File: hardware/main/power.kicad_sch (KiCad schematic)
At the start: 32 parts, among them Q1 SSM3J338R, Q2 BCP53, Q3 SSM3J338R, Q4 BC817, Q5 SSM3J338R, Q6 BC807, Q7 BC817, Q8 SSM3J338R, U5 AP2114H-3.3, U7 LM358

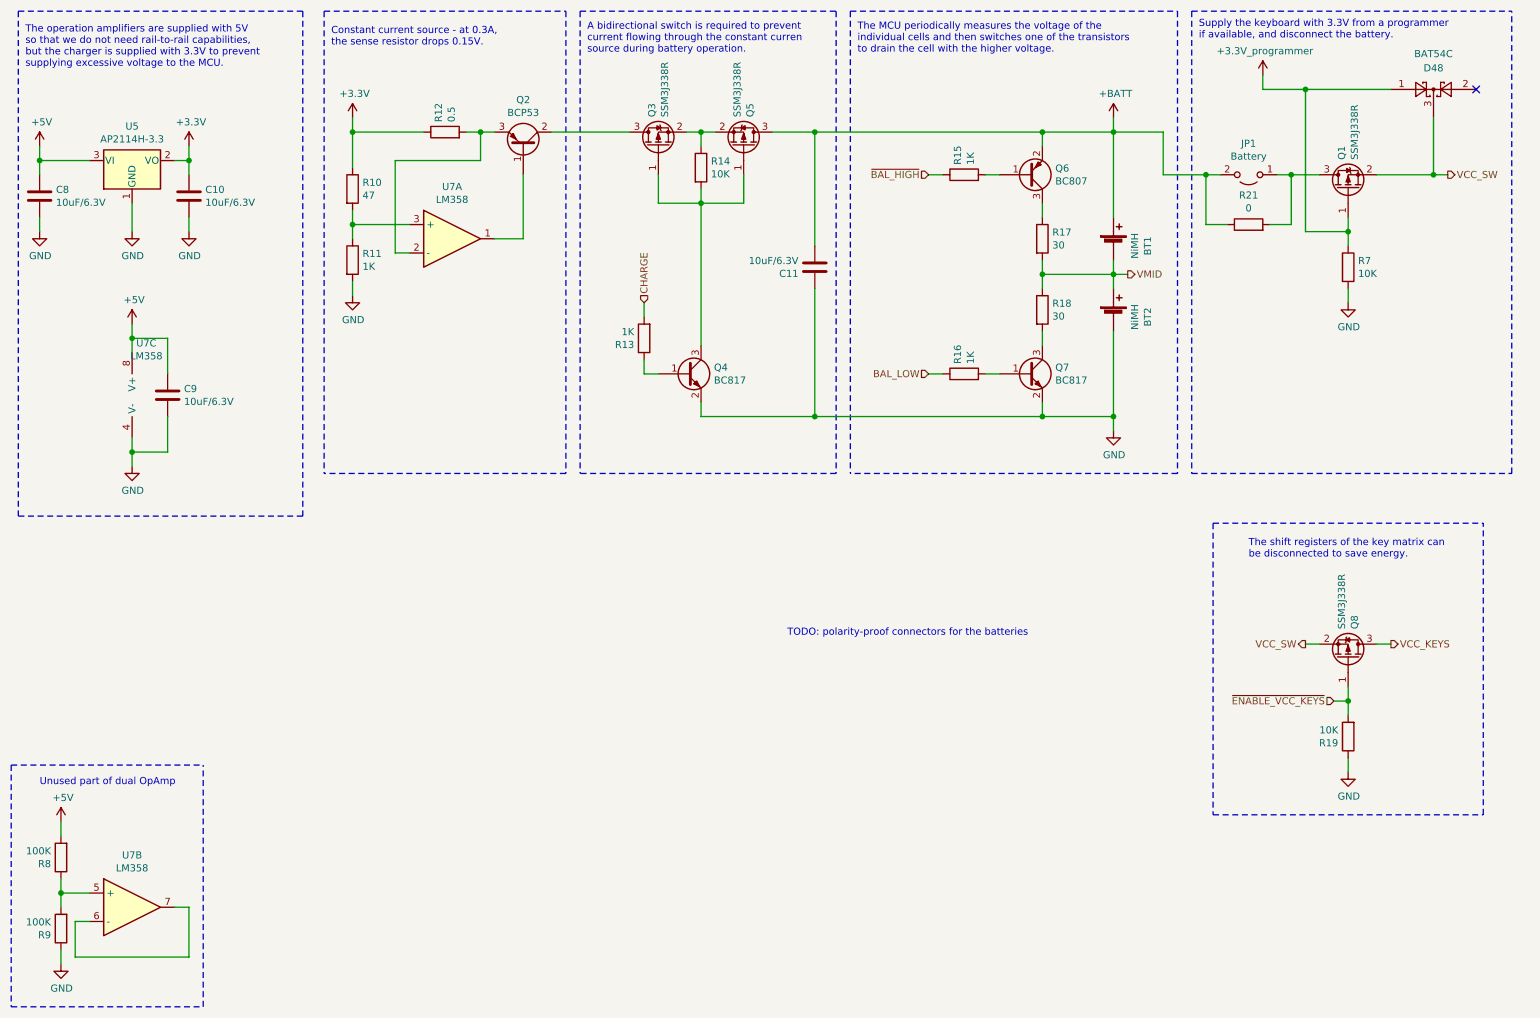
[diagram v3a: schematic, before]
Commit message: Rework the connection to the numpad
Changes:
- The UART lines now have a protection circuit
- The power supply line of the numpad can be switched on and off by the MCU.
- An Id-line is added so that the MCU can detect when the numpad is
  connected.
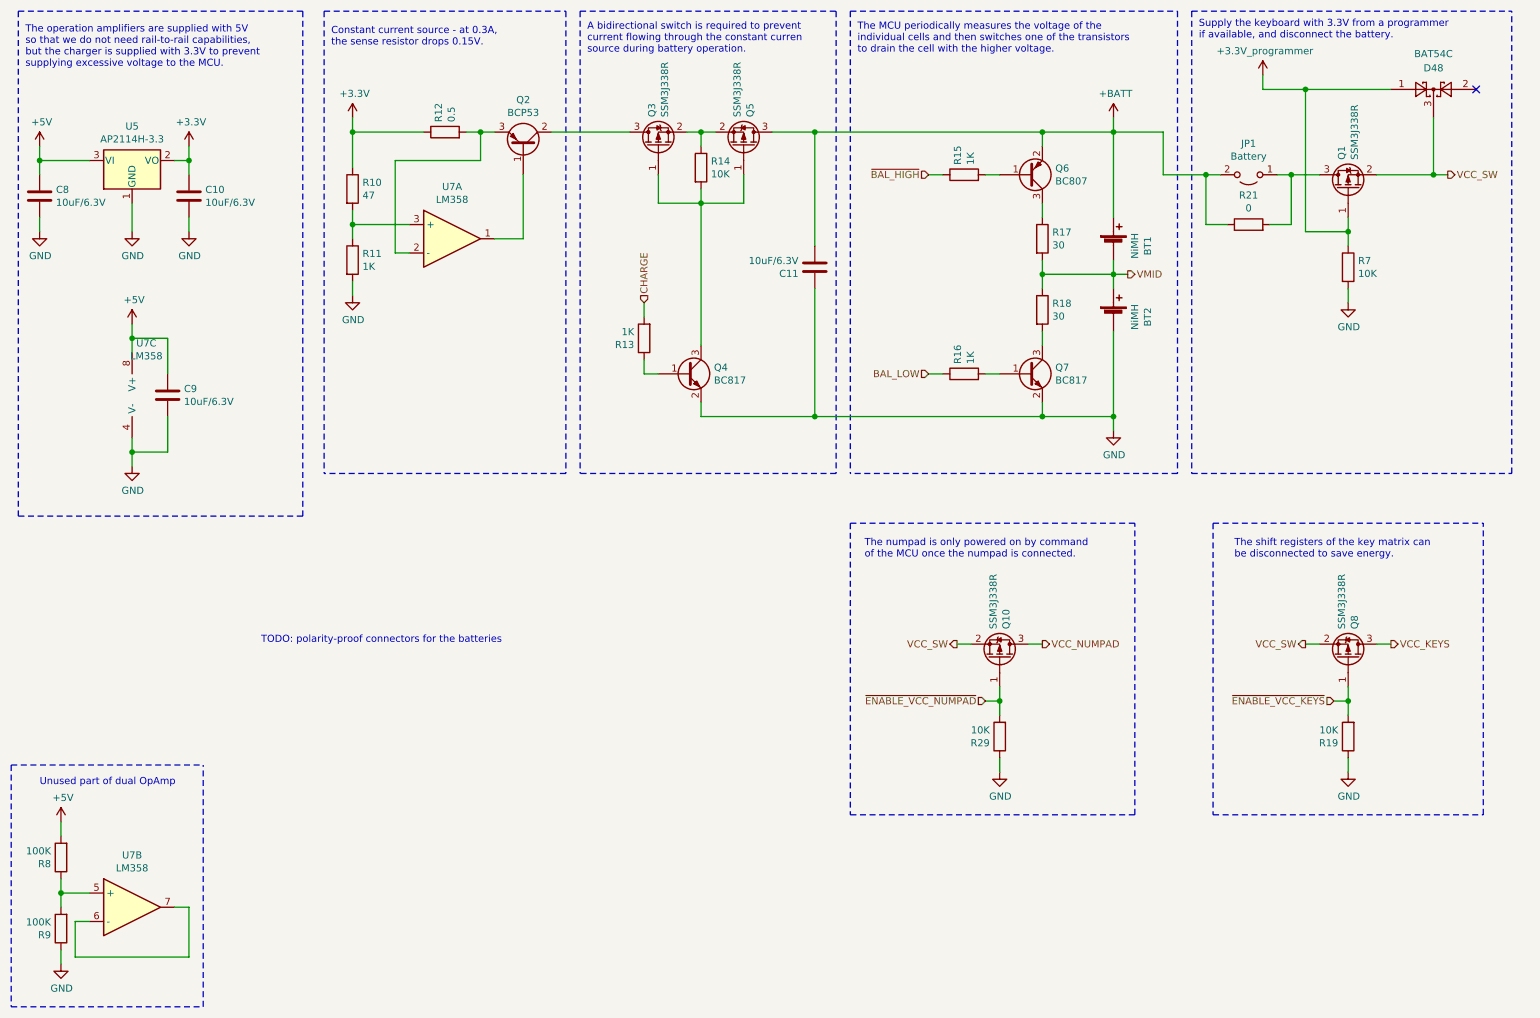
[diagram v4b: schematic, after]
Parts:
- added Q10: SSM3J338R, Package_TO_SOT_SMD:SOT-23_Handsoldering, symbol Device:Q_PMOS_GSD
- added R29: 10K, Resistor_SMD:R_0603_1608Metric, symbol Device:R
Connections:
- net GND: now also R29.1
- net VCC_SW: now also Q10.2 (S)
- new net VCC_NUMPAD: Q10.3 (D)
- new net ~ENABLE_VCC_NUMPAD: Q10.1 (G), R29.2
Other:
- note added: "The numpad is only powered on by command of the MCU once the numpad is connected."
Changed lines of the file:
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@@
   (junction (at 157.48 39.37) (diameter 1.016) (color 0 0 0 0))
   (junction (at 157.48 90.17) (diameter 1.016) (color 0 0 0 0))
+  (junction (at 190.5 140.97) (diameter 1.016) (color 0 0 0 0))
   (junction (at 198.12 39.37) (diameter 1.016) (color 0 0 0 0))
   (junction (at 198.12 64.77) (diameter 1.016) (color 0 0 0 0))
@@
     (stroke (width 0) (type solid) (color 0 0 0 0))
   )
+  (wire (pts (xy 182.88 130.81) (xy 185.42 130.81))
+    (stroke (width 0) (type solid) (color 0 0 0 0))
+  )
   (wire (pts (xy 187.96 46.99) (xy 190.5 46.99))
     (stroke (width 0) (type solid) (color 0 0 0 0))
@@
     (stroke (width 0) (type solid) (color 0 0 0 0))
   )
+  (wire (pts (xy 187.96 140.97) (xy 190.5 140.97))
+    (stroke (width 0) (type solid) (color 0 0 0 0))
+  )
+  (wire (pts (xy 190.5 138.43) (xy 190.5 140.97))
+    (stroke (width 0) (type solid) (color 0 0 0 0))
+  )
+  (wire (pts (xy 190.5 140.97) (xy 190.5 143.51))
+    (stroke (width 0) (type solid) (color 0 0 0 0))
+  )
+  (wire (pts (xy 190.5 151.13) (xy 190.5 153.67))
+    (stroke (width 0) (type solid) (color 0 0 0 0))
+  )
+  (wire (pts (xy 195.58 130.81) (xy 198.12 130.81))
+    (stroke (width 0) (type solid) (color 0 0 0 0))
+  )
   (wire (pts (xy 198.12 39.37) (xy 210.82 39.37))
     (stroke (width 0) (type solid) (color 0 0 0 0))
@@
   )
   (polyline (pts (xy 163.83 17.78) (xy 222.25 17.78))
+    (stroke (width 0) (type dash) (color 0 0 0 0))
+  )
+  (polyline (pts (xy 163.83 109.22) (xy 163.83 161.29))
+    (stroke (width 0) (type dash) (color 0 0 0 0))
+  )
+  (polyline (pts (xy 163.83 109.22) (xy 214.63 109.22))
+    (stroke (width 0) (type dash) (color 0 0 0 0))
+  )
+  (polyline (pts (xy 163.83 161.29) (xy 214.63 161.29))
+    (stroke (width 0) (type dash) (color 0 0 0 0))
+  )
+  (polyline (pts (xy 214.63 161.29) (xy 214.63 109.22))
     (stroke (width 0) (type dash) (color 0 0 0 0))
   )
@@
     (effects (font (size 1.27 1.27)) (justify left bottom))
   )
+  (text "TODO: polarity-proof connectors for the batteries" (at 101.6 130.81 180)
+    (effects (font (size 1.27 1.27)) (justify right bottom))
+  )
   (text "A bidirectional switch is required to prevent\ncurrent flowing through the constant curren\nsource during battery operation."
     (at 116.84 25.4 0)
@@
     (effects (font (size 1.27 1.27)) (justify left bottom))
   )
-  (text "TODO: polarity-proof connectors for the batteries" (at 195.58 129.54 180)
-    (effects (font (size 1.27 1.27)) (justify right bottom))
+  (text "The numpad is only powered on by command\nof the MCU once the numpad is connected."
+    (at 166.37 115.57 0)
+    (effects (font (size 1.27 1.27)) (justify left bottom))
   )
   (text "Supply the keyboard with 3.3V from a programmer\nif available, and disconnect the battery."
@@
   )
   (text "The shift registers of the key matrix can\nbe disconnected to save energy."
-    (at 234.95 115.57 0)
+    (at 232.41 115.57 0)
     (effects (font (size 1.27 1.27)) (justify left bottom))
   )
@@
     (effects (font (size 1.27 1.27)) (justify right))
   )
+  (hierarchical_label "VCC_SW" (shape output) (at 182.88 130.81 180)
+    (effects (font (size 1.27 1.27)) (justify right))
+  )
+  (hierarchical_label "~ENABLE_VCC_NUMPAD" (shape input) (at 187.96 140.97 180)
+    (effects (font (size 1.27 1.27)) (justify right))
+  )
+  (hierarchical_label "VCC_NUMPAD" (shape output) (at 198.12 130.81 0)
+    (effects (font (size 1.27 1.27)) (justify left))
+  )
   (hierarchical_label "VMID" (shape output) (at 213.36 64.77 0)
     (effects (font (size 1.27 1.27)) (justify left))
@@
     )
   )
+  (symbol (lib_id "power:GND") (at 190.5 153.67 0) (unit 1)
+    (in_bom yes) (on_board yes)
+    (property "Reference" "#PWR0140" (id 0) (at 190.5 160.02 0)
+      (effects (font (size 1.27 1.27)) hide)
+    )
+    (property "Value" "GND" (id 1) (at 190.6143 157.9944 0))
+    (property "Footprint" "" (id 2) (at 190.5 153.67 0)
+      (effects (font (size 1.27 1.27)) hide)
+    )
+    (property "Datasheet" "" (id 3) (at 190.5 153.67 0)
+      (effects (font (size 1.27 1.27)) hide)
+    )
+  )
   (symbol (lib_id "power:GND") (at 210.82 92.71 0) (unit 1)
     (in_bom yes) (on_board yes)
@@
     )
     (property "Datasheet" "~" (id 3) (at 184.15 82.55 0)
+      (effects (font (size 1.27 1.27)) hide)
+    )
+  )
+  (symbol (lib_id "Device:R") (at 190.5 147.32 180) (unit 1)
+    (in_bom yes) (on_board yes)
+    (property "Reference" "R29" (id 0) (at 188.7219 148.4694 0)
+      (effects (font (size 1.27 1.27)) (justify left))
+    )
+    (property "Value" "10K" (id 1) (at 188.722 146.171 0)
+      (effects (font (size 1.27 1.27)) (justify left))
+    )
+    (property "Footprint" "Resistor_SMD:R_0603_1608Metric" (id 2) (at 192.278 147.32 90)
+      (effects (font (size 1.27 1.27)) hide)
+    )
+    (property "Datasheet" "~" (id 3) (at 190.5 147.32 0)
       (effects (font (size 1.27 1.27)) hide)
     )
@@
       (effects (font (size 1.27 1.27)) hide)
     )
+  )
+  (symbol (lib_id "Device:Q_PMOS_GSD") (at 190.5 133.35 270) (mirror x) (unit 1)
+    (in_bom yes) (on_board yes)
+    (property "Reference" "Q10" (id 0) (at 191.6494 128.1429 0)
+      (effects (font (size 1.27 1.27)) (justify left))
+    )
+    (property "Value" "SSM3J338R" (id 1) (at 189.351 128.143 0)
+      (effects (font (size 1.27 1.27)) (justify left))
+    )
+    (property "Footprint" "Package_TO_SOT_SMD:SOT-23_Handsoldering" (id 2) (at 193.04 128.27 0)
+      (effects (font (size 1.27 1.27)) hide)
+    )
+    (property "Datasheet" "~" (id 3) (at 190.5 133.35 0)
+      (effects (font (size 1.27 1.27)) hide)
+    )
+    (property "Part Name" "Toshiba SSM3J338R" (id 4) (at 190.5 133.35 0)
+      (effects (font (size 1.27 1.27)) hide)
+    )
+    (property "Mouser" "757-SSM3J338RLF" (id 5) (at 190.5 133.35 0)
+      (effects (font (size 1.27 1.27)) hide)
+    )
